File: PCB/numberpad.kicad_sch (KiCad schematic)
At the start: 40 parts, among them J1 Light_Sensor, J2 Rotary_Encoder, J3 Screen_Connector, J4 FingerPrint, SW0 0, SW1 ., SW10 8, SW11 9, SW12 +, SW13 num_lock, SW14 /, SW15 *, SW16 -, SW2 1, SW3 2, SW4 3, SW5 enter, SW6 4, SW7 5, SW8 6, SW9 7, U1 ATmega328-P, U2 ESP32-S3-DEVKITC-1-N8R2

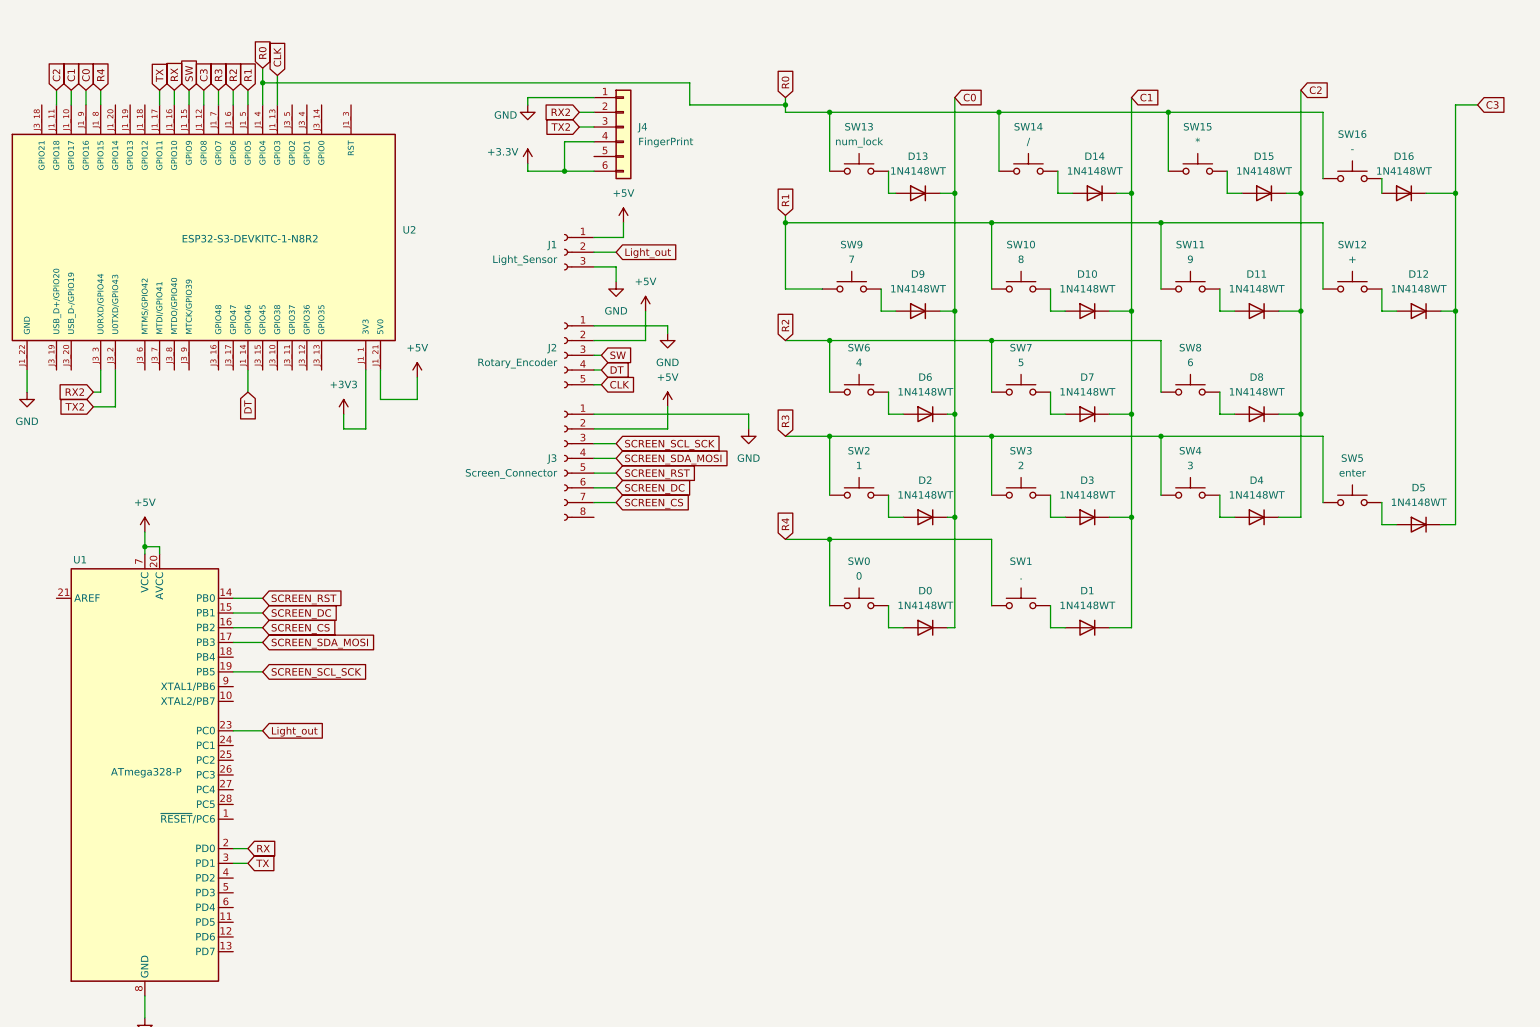
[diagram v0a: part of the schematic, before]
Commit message: update screen support now display information for the screen + brightness.
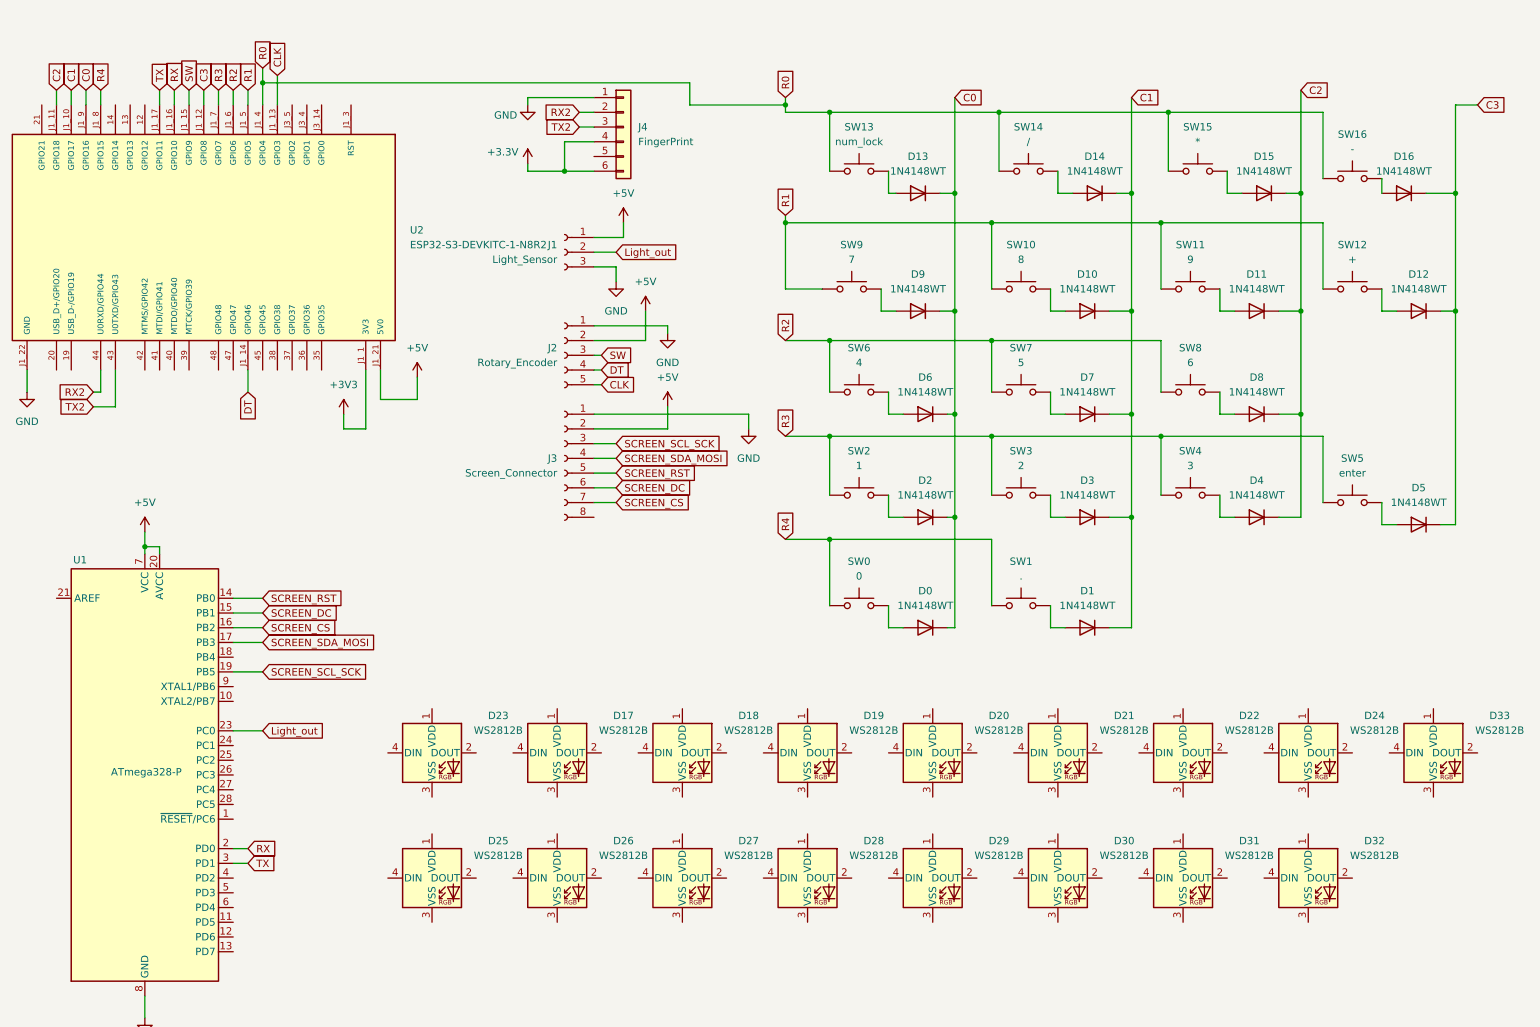
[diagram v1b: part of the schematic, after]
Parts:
- added D17, D18, D19, D20, D21, D22, D23, D24, D25, D26, D27, D28, D29, D30, D31, D32, D33: WS2812B, LED_SMD:LED_WS2812B_PLCC4_5.0x5.0mm_P3.2mm, symbol LED:WS2812B
- U2: footprint PCM_Espressif:ESP32-S3-DevKitC -> ESP32-S3-DEVKITC-1-N8R2:XCVR_ESP32-S3-DEVKITC-1-N8R2
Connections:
- net RX2: now also U2.44 (U0RXD/GPIO44); no longer U2.J3_3 (U0RXD/GPIO44)
- net TX2: now also U2.43 (U0TXD/GPIO43); no longer U2.J3_2 (U0TXD/GPIO43)

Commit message: Windows support !
Windows HID support have been added in this version also working with Android. Both only work with default keymap.
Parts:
- removed D17, D18, D19, D20, D21, D22, D23, D24, D25, D26, D27, D28, D29, D30, D31, D32, D33: WS2812B, LED_SMD:LED_WS2812B_PLCC4_5.0x5.0mm_P3.2mm, symbol LED:WS2812B
- removed U2: ESP32-S3-DEVKITC-1-N8R2, ESP32-S3-DEVKITC-1-N8R2:XCVR_ESP32-S3-DEVKITC-1-N8R2, symbol ESP32-S3-DEVKITC-1-N8R2:ESP32-S3-DEVKITC-1-N8R2
- added 3V3, 5V1: Conn_01x02_Pin, Connector_PinHeader_2.54mm:PinHeader_1x02_P2.54mm_Vertical, symbol Connector:Conn_01x02_Pin
- added D17, D18, D19, D20, D21, D22, D23, D24, D25, D26, D27, D28, D29, D30, D31, D32, D33: SK6812MINI, footprints:LED_SK6812-E, symbol SK6812-E:SK6812-E
- added J5: USB_A, Connector_USB:USB_A_Kycon_KUSBX-AS1N-B_Horizontal, symbol Connector:USB_A
- added J6: Programmer, Connector_PinSocket_2.54mm:PinSocket_1x08_P2.54mm_Horizontal, symbol Connector:Conn_01x08_Pin
- added S1: MINI-SPDT-SW, footprints:SW_MINI-SPDT-SW, symbol MINI-SPDT-SW:MINI-SPDT-SW
- added U2: ESP32-S3-DEVKITC-1-N16R8V, footprints:XCVR_ESP32-S3-DEVKITC-1-N8R2, symbol ESP32-S3-DEVKITC-1-N16R8V:ESP32-S3-DEVKITC-1-N16R8V
- J4: value FingerPrint -> FingerPrint_UART
- SW0, SW1, SW10, SW11, SW12, SW13, SW14, SW15, SW16, SW2, SW3, SW4, SW5, SW6, SW7, SW8, SW9: footprint footprints:SW_Gateron_LowProfile_THT -> footprints:SW_Gateron_LowProfile_HotSwap_PTH
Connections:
- net +3.3V is gone; now on net +3V3: J4.4 (Pin_4), J4.6 (Pin_6)
- net +3V3: now also 3V3.1 (Pin_1), U2.J1_1 (3V3), U2.J1_2 (3V3)
- net +5V: now also 5V1.1 (Pin_1), D17.1 (VDD), D18.1 (VDD), D19.1 (VDD), D20.1 (VDD), D21.1 (VDD), D22.1 (VDD), D23.1 (VDD), D24.1 (VDD), D25.1 (VDD), D26.1 (VDD), D27.1 (VDD), D28.1 (VDD), D29.1 (VDD), D30.1 (VDD), D31.1 (VDD), D32.1 (VDD), D33.1 (VDD), J5.1 (VBUS), J6.2 (Pin_2), S1.1, S1.2, S1.3, U2.J1_21 (5V0)
- net C0: now also U2.J1_9 (GPIO16)
- net C1: now also U2.J1_10 (GPIO17)
- net C2: now also U2.J1_11 (GPIO18)
- net C3: now also U2.J1_12 (GPIO8)
- net CLK: now also U2.J1_13 (GPIO3)
- net DT: now also U2.J1_14 (GPIO46)
- net GND: now also 3V3.2 (Pin_2), 5V1.2 (Pin_2), D17.3 (GND), D18.3 (GND), D19.3 (GND), D20.3 (GND), D21.3 (GND), D22.3 (GND), D23.3 (GND), D24.3 (GND), D25.3 (GND), D26.3 (GND), D27.3 (GND), D28.3 (GND), D29.3 (GND), D30.3 (GND), D31.3 (GND), D32.3 (GND), D33.3 (GND), J5.4 (GND), J5.5 (Shield), J6.3 (Pin_3), U2.J1_22 (GND), U2.J3_1 (GND), U2.J3_21 (GND), U2.J3_22 (GND)
- net R0: now also U2.J1_4 (GPIO4)
- net R1: now also U2.J1_5 (GPIO5)
- net R2: now also U2.J1_6 (GPIO6)
- net R3: now also U2.J1_7 (GPIO7)
- net R4: now also U2.J1_8 (GPIO15)
- net RX: now also U2.J1_16 (GPIO10)
- net RX2: now also U2.J3_3 (U0RXD/GPIO44)
- net SW: now also U2.J1_15 (GPIO9)
- net TX: now also U2.J1_17 (GPIO11)
- net TX2: now also U2.J3_2 (U0TXD/GPIO43)
- net PC6: now reaches U1.1 (~{RESET}/PC6)
- net PC6: now also J6.6 (Pin_6)
- net PB4: now reaches U1.18 (PB4)
- net PB4: now also J6.4 (Pin_4)
- net Light_out renamed Light_in
- net Light_in: no longer J1.2 (Pin_2)
- net SCREEN_SCL_SCK renamed PB5
- net PB5: now also J6.5 (Pin_5)
- net SCREEN_SDA_MOSI renamed PB3
- net PB3: now also J6.7 (Pin_7)
- new net: D24.2 (DOUT), D25.4 (DIN)
- new net: D23.2 (DOUT), D24.4 (DIN)
- new net: D28.2 (DOUT), D29.4 (DIN)
- new net: D27.2 (DOUT), D28.4 (DIN)
- new net: D26.2 (DOUT), D27.4 (DIN)
- new net: D31.2 (DOUT), D32.4 (DIN)
- new net: D30.2 (DOUT), D31.4 (DIN)
- new net: D32.2 (DOUT), D33.4 (DIN)
- new net: D21.2 (DOUT), D22.4 (DIN)
- new net: D20.2 (DOUT), D21.4 (DIN)
- new net: D17.2 (DOUT), D18.4 (DIN)
- new net: D19.2 (DOUT), D20.4 (DIN)
- new net D+: J5.3 (D+), U2.J3_19 (USB_D+/GPIO20)
- new net D-: J5.2 (D-), U2.J3_20 (USB_D-/GPIO19)
- new net LEDS_Out: D17.4 (DIN), U2.J3_16 (GPIO48)
- new net Light_int: J1.2 (Pin_2)
- new net R0_LED: D18.2 (DOUT), D19.4 (DIN)
- new net R1_LED: D22.2 (DOUT), D23.4 (DIN)
- new net R2_LED: D25.2 (DOUT), D26.4 (DIN)
- new net R3_LED: D29.2 (DOUT), D30.4 (DIN)
- new net RST: U2.J1_3 (RST)
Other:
- added sheet Key_Switches Sheet (Switch.kicad_sch)
- added sheet LED (LED.kicad_sch)
- note added: "1.9" IPS SCREEN 320x170px RGB SPI"
- note added: "Accessories"
- note added: "Atmega328P + PicKit4"
- note added: "ESP32 S3 DevKit"
- note added: "Light Sensor TEMT6000"
- note added: "UART FingerPrint Sensor Connector"
- note added: "USB A Port for USB passtrought + Fingerprint sensor"
- note added: "Volume Knob Using Rotary Encoder"
- moved on the sheet: D0, D1, D10, D11, D12, D13, D14, D15, D16, D2, D3, D4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

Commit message: update to support volume on android + update screen. missing device connected name + last key pressed
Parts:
- added C1, C2: 100nF, Capacitor_THT:C_Rect_L4.6mm_W2.0mm_P2.50mm_MKS02_FKP02, symbol Device:C
- added J7: USB_C_TO_PC, Connector_PinHeader_1.00mm:PinHeader_1x04_P1.00mm_Vertical, symbol Connector:Conn_01x04_Pin
- added R1: 10K, Resistor_THT:R_Axial_DIN0204_L3.6mm_D1.6mm_P7.62mm_Horizontal, symbol Device:R_US
- added R2: 12K1, Resistor_THT:R_Axial_DIN0204_L3.6mm_D1.6mm_P7.62mm_Horizontal, symbol Device:R_US
- added U3: USB2514B_Bi, Package_DFN_QFN:QFN-36-1EP_6x6mm_P0.5mm_EP3.7x3.7mm, symbol Interface_USB:USB2514B_Bi
- added Y1: Crystal_Small, Crystal:Crystal_HC18-U_Vertical, symbol Device:Crystal_Small
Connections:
- net +5V: now also J7.1 (Pin_1)
- net D+: now also J7.3 (Pin_3), U3.31 (USBDP_UP); no longer J5.3 (D+), U2.J3_19 (USB_D+/GPIO20)
- net D-: now also J7.2 (Pin_2), U3.30 (USBDM_UP); no longer J5.2 (D-), U2.J3_20 (USB_D-/GPIO19)
- net GND: now also C1.2, C2.2, J7.4 (Pin_4), R2.1, U3.37 (VSS)
- new net: R1.2, U3.26 (RESET_N)
- new net: U3.32 (XTALOUT), Y1.1
- new net: U3.33 (XTALIN/CLKIN), Y1.2
- new net: C2.1, U3.14 (CRFILT)
- new net: C1.1, U3.34 (PLLFILT)
- new net: R2.2, U3.35 (RBIAS)
- new net +3.3V: R1.1, U3.10 (VDDA33), U3.15 (VDD33), U3.23 (VDD33), U3.29 (VDDA33), U3.36 (VDDA33), U3.5 (VDDA33)
- new net DE+: U2.J3_19 (USB_D+/GPIO20), U3.2 (USBDP_DN1/PRT_DIS_P1)
- new net DE-: U2.J3_20 (USB_D-/GPIO19), U3.1 (USBDM_DN1/PRT_DIS_M1)
- new net DS+: J5.3 (D+), U3.4 (USBDP_DN2/PRT_DIS_P2)
- new net DS-: J5.2 (D-), U3.3 (USBDM_DN2/PRT_DIS_M2)
